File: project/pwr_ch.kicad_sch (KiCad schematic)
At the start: 15 parts, among them J201 XT-IN, J202 METER, J203 XT-OUT, Q201 AON6144, U201 UCC27517DBVR

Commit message: finalizing design
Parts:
- added TP201: TP_GND, TestPoint:TestPoint_Pad_D2.5mm, symbol Connector:TestPoint_Flag
- C201, C202, C203: lcsc# (none) -> C476766
- D201: lcsc# (none) -> C1884542
- Q201: lcsc# (none) -> C133142
- U201: lcsc# (none) -> C20623191
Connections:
- net PGND: now also TP201.1
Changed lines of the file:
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@@
   (title_block
     (title "DZF-6020-UV-power-addon / power board")
-    (date "2024-08-30")
+    (date "2024-09-02")
     (rev "1.0")
   )
@@
   (junction (at 176.53 109.22) (diameter 0) (color 0 0 0 0)
   )
+  (junction (at 116.84 114.3) (diameter 0) (color 0 0 0 0)
+  )
   (junction (at 144.78 114.3) (diameter 0) (color 0 0 0 0)
   )
@@
     (stroke (width 0) (type default) (color 0 0 0 0))
   )
+  (wire (pts (xy 116.84 114.3) (xy 114.3 114.3))
+    (stroke (width 0) (type default) (color 0 0 0 0))
+  )
   (wire (pts (xy 201.93 114.3) (xy 207.01 114.3))
     (stroke (width 0) (type default) (color 0 0 0 0))
@@
     (stroke (width 0) (type default) (color 0 0 0 0))
   )
-  (wire (pts (xy 119.38 114.3) (xy 114.3 114.3))
+  (wire (pts (xy 119.38 114.3) (xy 116.84 114.3))
     (stroke (width 0) (type default) (color 0 0 0 0))
   )
@@
     )
     (property "Datasheet" "~" (id 3) (at 119.38 118.11 0)
+      (effects (font (size 1.27 1.27)) hide)
+    )
+    (property "lcsc#" "C476766" (id 4) (at 119.38 118.11 0)
       (effects (font (size 1.27 1.27)) hide)
     )
@@
       (effects (font (size 1.27 1.27)) (justify left) hide)
     )
+    (property "lcsc#" "C133142" (id 4) (at 173.99 104.14 0)
+      (effects (font (size 1.27 1.27)) hide)
+    )
     (pin "1")
     (pin "2")
@@
       (effects (font (size 1.27 1.27)) hide)
     )
+    (property "lcsc#" "C20623191" (id 4) (at 144.78 106.68 0)
+      (effects (font (size 1.27 1.27)) hide)
+    )
     (pin "1")
     (pin "2")
@@
     (pin "2")
   )
+  (symbol (lib_id "Connector:TestPoint_Flag") (at 116.84 114.3 0) (unit 1)
+    (in_bom no) (on_board yes)
+    (property "Reference" "TP201" (id 0) (at 116.84 110.49 0)
+      (effects (font (size 1.27 1.27)) (justify left))
+    )
+    (property "Value" "TP_GND" (id 1) (at 124.46 114.1729 0)
+      (effects (font (size 1.27 1.27)) (justify left) hide)
+    )
+    (property "Footprint" "TestPoint:TestPoint_Pad_D2.5mm" (id 2) (at 121.92 114.3 0)
+      (effects (font (size 1.27 1.27)) hide)
+    )
+    (property "Datasheet" "~" (id 3) (at 121.92 114.3 0)
+      (effects (font (size 1.27 1.27)) hide)
+    )
+    (pin "1")
+  )
   (symbol (lib_id "Connector_Generic:Conn_01x03") (at 97.79 102.87 0) (unit 1)
     (in_bom yes) (on_board yes) (fields_autoplaced)
@@
     )
     (property "Datasheet" "~" (id 3) (at 109.22 106.68 0)
+      (effects (font (size 1.27 1.27)) hide)
+    )
+    (property "lcsc#" "C476766" (id 4) (at 109.22 106.68 0)
       (effects (font (size 1.27 1.27)) hide)
     )
@@
       (effects (font (size 1.27 1.27)) hide)
     )
+    (property "lcsc#" "C1884542" (id 4) (at 189.23 105.41 0)
+      (effects (font (size 1.27 1.27)) hide)
+    )
     (pin "1")
     (pin "2")
@@
       (effects (font (size 1.27 1.27)) hide)
     )
+    (property "lcsc#" "C476766" (id 4) (at 189.23 97.79 0)
+      (effects (font (size 1.27 1.27)) hide)
+    )

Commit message: fixing a lot of stuff in power board
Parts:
- removed C204: DNP, Capacitor_SMD:C_0805_2012Metric_Pad1.18x1.45mm_HandSolder, symbol Device:C
- removed R205: 0, Resistor_SMD:R_0805_2012Metric_Pad1.20x1.40mm_HandSolder, symbol Device:R
- added C201, C203, C205: 10u/35v, Capacitor_SMD:C_1206_3216Metric_Pad1.33x1.80mm_HandSolder, symbol Device:C
- C202: value 100n -> 10u/35v; footprint Capacitor_SMD:C_0805_2012Metric_Pad1.18x1.45mm_HandSolder -> Capacitor_SMD:C_1206_3216Metric_Pad1.33x1.80mm_HandSolder; lcsc# C476766 -> C92797
- D201: value DS14W -> SS34A; footprint Diode_SMD:D_SOD-123F -> Diode_SMD:D_SMA; lcsc# C1884542 -> C2886580
- R201: value 10K -> 10R
- R203: value 43R -> 33R
- renumbered C201 to C204, C203 to C206
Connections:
- net snub is gone; now on net Vcc: C206.1, D201.1 (K)
- net GND: no longer C202.2
- net IN-: now also C202.2, C201.2, C203.1
- net PGND: now also C203.2, C205.2; no longer C202.1
- net Vcc: now also C202.1, C201.1, C205.1
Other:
- moved on the sheet: C204, C206, J201, J202, J203, Q201, R201, R202, R203, R204, TP201, U201

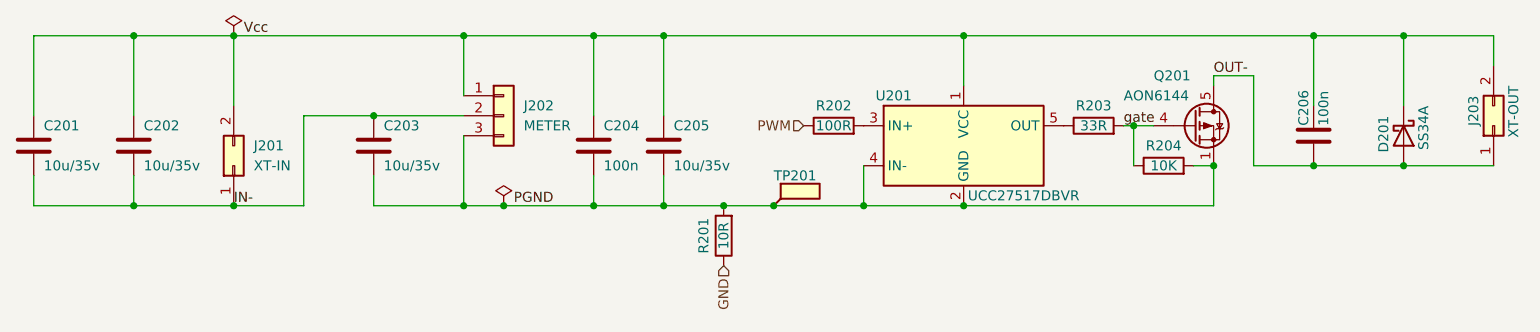
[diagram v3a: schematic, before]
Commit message: using isolated gate driver
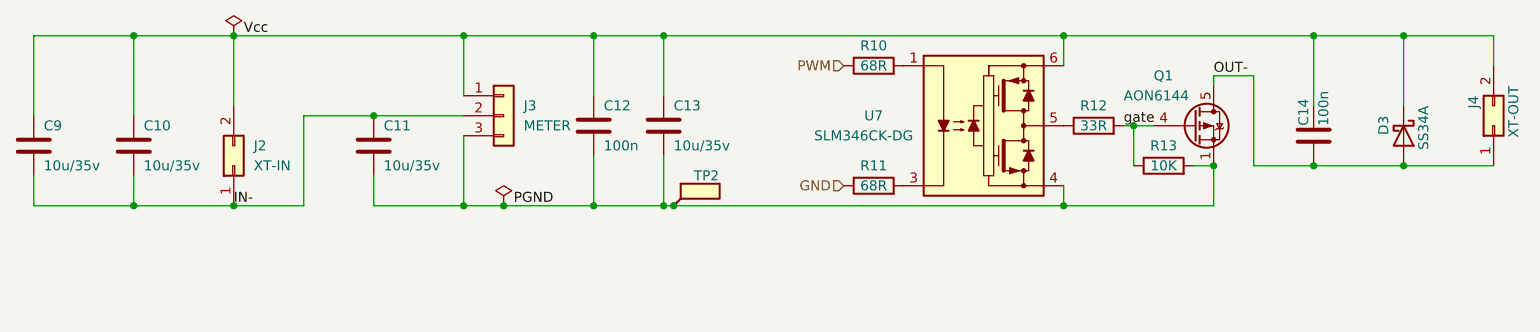
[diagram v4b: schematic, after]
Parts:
- removed R201: 10R, Resistor_SMD:R_0805_2012Metric_Pad1.20x1.40mm_HandSolder, symbol Device:R
- removed R202: 100R, Resistor_SMD:R_0805_2012Metric_Pad1.20x1.40mm_HandSolder, symbol Device:R
- removed U201: UCC27517DBVR, Package_TO_SOT_SMD:SOT-23-5_HandSoldering, symbol -local:UCC27517DBVR
- added R10, R11: 68R, Resistor_SMD:R_0805_2012Metric_Pad1.20x1.40mm_HandSolder, symbol Device:R
- added U7: SLM346CK-DG, Package_SO:SSO-6_6.8x4.6mm_P1.27mm_Clearance8mm, symbol Driver_FET:ACPL-W343
- renumbered C202 to C10, C203 to C11, C204 to C12, C205 to C13, C206 to C14, C201 to C9, D201 to D3, J201 to J2, J202 to J3, J203 to J4, Q201 to Q1, R203 to R12, R204 to R13, TP201 to TP2
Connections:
- net GND: now also R11.1
- net PGND: now also U7.4 (VEE)
- net PWM: now also R10.1
- net Vcc: now also U7.6 (VCC)
- net at R12.1: now also U7.5 (VO)
- new net: R10.2, U7.1 (A)
- new net: R11.2, U7.3 (C)
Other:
- moved on the sheet: C12, C13, TP2
